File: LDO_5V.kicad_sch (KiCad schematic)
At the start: 36 parts, among them Q1601 NMOS, Q1602 NMOS, Q1603 NMOS, U1601 TPS62933, U1602 TPS62933, U1603 LM74700, U1604 LM74700

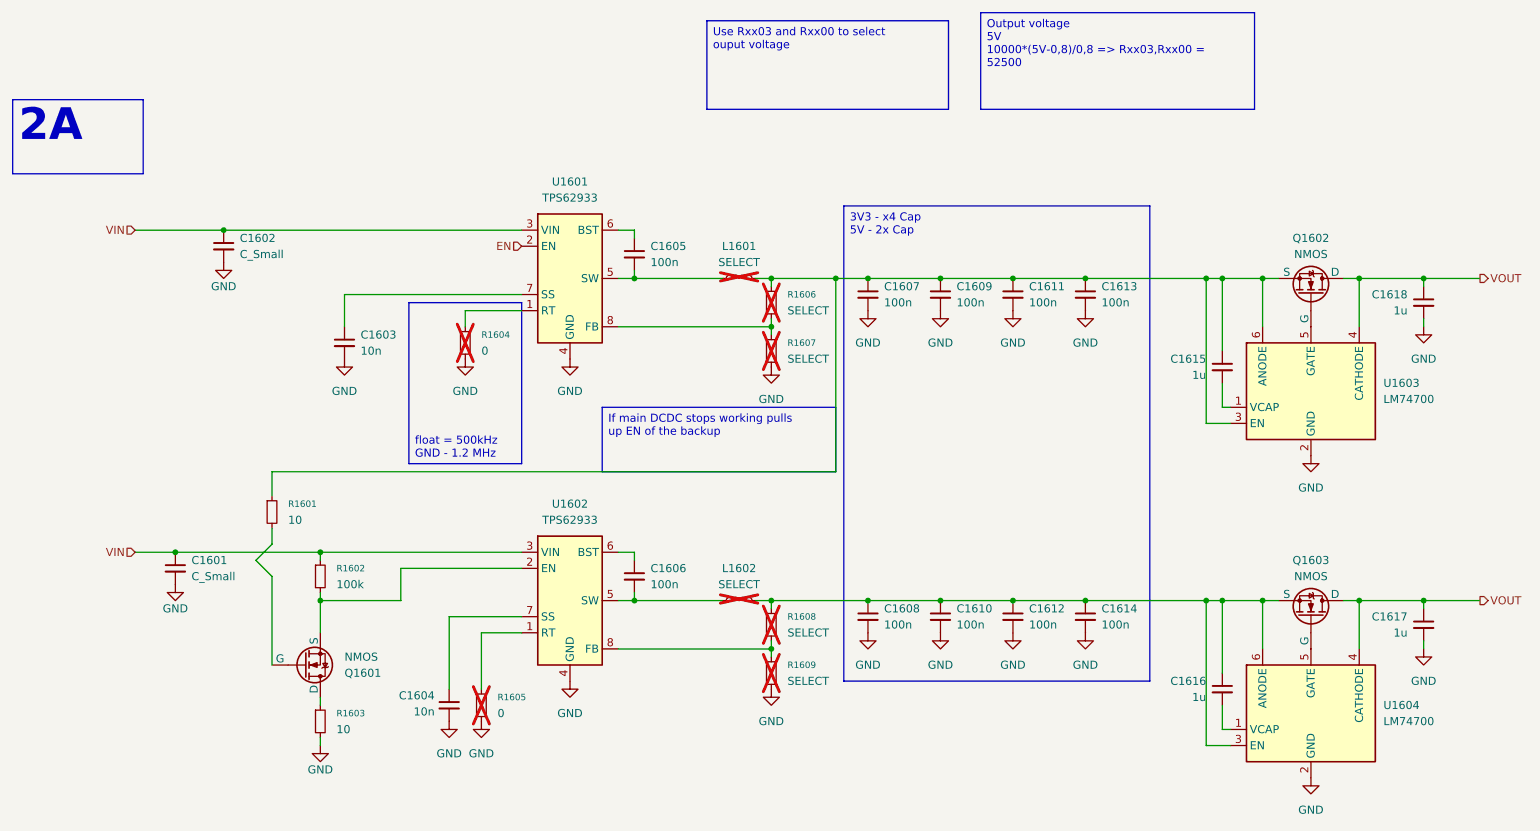
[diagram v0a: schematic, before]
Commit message: wired channel alerts; added schematic for test pbc
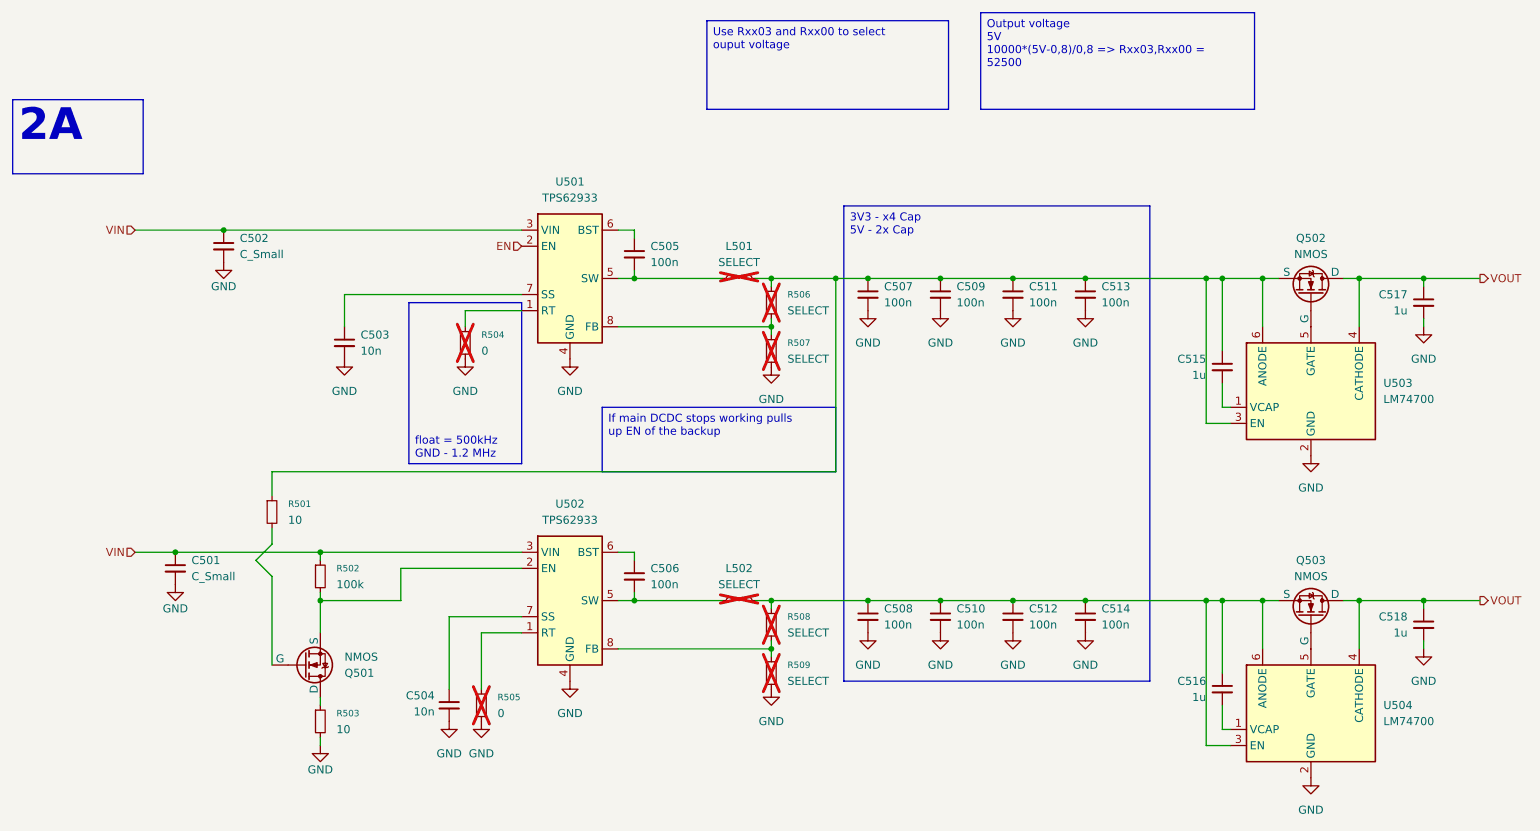
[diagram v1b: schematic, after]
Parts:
- removed C1601, C1602: C_Small, Capacitor_SMD:C_0603_1608Metric_Pad1.08x0.95mm_HandSolder, symbol Device:C_Small
- removed C1603, C1604: 10n, Capacitor_SMD:C_0603_1608Metric_Pad1.08x0.95mm_HandSolder, symbol Device:C_Small
- removed C1605, C1606, C1607, C1608, C1609, C1610, C1611, C1612, C1613, C1614: 100n, Capacitor_SMD:C_0603_1608Metric_Pad1.08x0.95mm_HandSolder, symbol Device:C_Small
- removed C1615, C1616, C1617, C1618: 1u, Capacitor_SMD:C_0603_1608Metric_Pad1.08x0.95mm_HandSolder, symbol Device:C_Small
- removed L1601, L1602: SELECT, Inductor_SMD:L_Taiyo-Yuden_NR-10050_9.8x10.0mm_HandSoldering, symbol Device:L_Small
- removed Q1601: NMOS, Package_TO_SOT_SMD:SOT-23, symbol Simulation_SPICE:NMOS
- removed Q1602, Q1603: NMOS, Package_TO_SOT_SMD:SOT-23-6, symbol Simulation_SPICE:NMOS
- removed R1601, R1603: 10, Resistor_SMD:R_0603_1608Metric_Pad0.98x0.95mm_HandSolder, symbol Device:R_Small
- removed R1602: 100k, Resistor_SMD:R_0603_1608Metric_Pad0.98x0.95mm_HandSolder, symbol Device:R_Small
- removed R1604, R1605: 0, Resistor_SMD:R_0603_1608Metric_Pad0.98x0.95mm_HandSolder, symbol Device:R_Small
- removed R1606, R1607, R1608, R1609: SELECT, Resistor_SMD:R_0603_1608Metric_Pad0.98x0.95mm_HandSolder, symbol Device:R_Small
- removed U1601, U1602: TPS62933, Package_TO_SOT_SMD:SOT-583-8, symbol Regulator_Switching:TPS62933
- removed U1603, U1604: LM74700, Package_TO_SOT_SMD:SOT-23-6, symbol Power_Management:LM74700
- added C501, C502: C_Small, Capacitor_SMD:C_0603_1608Metric_Pad1.08x0.95mm_HandSolder, symbol Device:C_Small
- added C503, C504: 10n, Capacitor_SMD:C_0603_1608Metric_Pad1.08x0.95mm_HandSolder, symbol Device:C_Small
- added C505, C506, C507, C508, C509, C510, C511, C512, C513, C514: 100n, Capacitor_SMD:C_0603_1608Metric_Pad1.08x0.95mm_HandSolder, symbol Device:C_Small
- added C515, C516, C517, C518: 1u, Capacitor_SMD:C_0603_1608Metric_Pad1.08x0.95mm_HandSolder, symbol Device:C_Small
- added L501, L502: SELECT, Inductor_SMD:L_Taiyo-Yuden_NR-10050_9.8x10.0mm_HandSoldering, symbol Device:L_Small
- added Q501: NMOS, Package_TO_SOT_SMD:SOT-23, symbol Simulation_SPICE:NMOS
- added Q502, Q503: NMOS, Package_TO_SOT_SMD:SOT-23-6, symbol Simulation_SPICE:NMOS
- added R501, R503: 10, Resistor_SMD:R_0603_1608Metric_Pad0.98x0.95mm_HandSolder, symbol Device:R_Small
- added R502: 100k, Resistor_SMD:R_0603_1608Metric_Pad0.98x0.95mm_HandSolder, symbol Device:R_Small
- added R504, R505: 0, Resistor_SMD:R_0603_1608Metric_Pad0.98x0.95mm_HandSolder, symbol Device:R_Small
- added R506, R507, R508, R509: SELECT, Resistor_SMD:R_0603_1608Metric_Pad0.98x0.95mm_HandSolder, symbol Device:R_Small
- added U501, U502: TPS62933, Package_TO_SOT_SMD:SOT-583-8, symbol Regulator_Switching:TPS62933
- added U503, U504: LM74700, Package_TO_SOT_SMD:SOT-23-6, symbol Power_Management:LM74700
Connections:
- net EN: now also U501.2 (EN)
- net GND: now also C501.2, C502.2, C503.2, C504.2, C507.2, C508.2, C509.2, C510.2, C511.2, C512.2, C513.2, C514.2, C517.2, C518.2, R503.2, R504.1, R505.1, R507.1, R509.1, U501.4 (GND), U502.4 (GND), U503.2 (GND), U504.2 (GND)
- net VIN: now also C501.1, C502.1, R502.1, U501.3 (VIN), U502.3 (VIN)
- net VOUT: now also C517.1, C518.1, Q502.1 (D), Q503.1 (D), U503.4 (CATHODE), U504.4 (CATHODE)
- new net: C508.1, C510.1, C512.1, C514.1, C516.1, L502.2, Q503.3 (S), R508.2, U504.3 (EN), U504.6 (ANODE)
- new net: C504.1, U502.7 (SS)
- new net: C503.1, U501.7 (SS)
- new net: R506.1, R507.2, U501.8 (FB)
- new net: Q501.3 (S), R502.2, U502.2 (EN)
- new net: Q503.2 (G), U504.5 (GATE)
- new net: C507.1, C509.1, C511.1, C513.1, C515.1, L501.2, Q502.3 (S), R501.1, R506.2, U503.3 (EN), U503.6 (ANODE)
- new net: C516.2, U504.1 (VCAP)
- new net: Q502.2 (G), U503.5 (GATE)
- new net: R504.2, U501.1 (RT)
- new net: R505.2, U502.1 (RT)
- new net: C506.2, L502.1, U502.5 (SW)
- new net: C506.1, U502.6 (BST)
- new net: R508.1, R509.2, U502.8 (FB)
- new net: Q501.1 (D), R503.1
- new net: Q501.2 (G), R501.2
- new net: C505.2, L501.1, U501.5 (SW)
- new net: C515.2, U503.1 (VCAP)
- new net: C505.1, U501.6 (BST)

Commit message: reduced number of DCDC converter for PV panels; updated test pcb
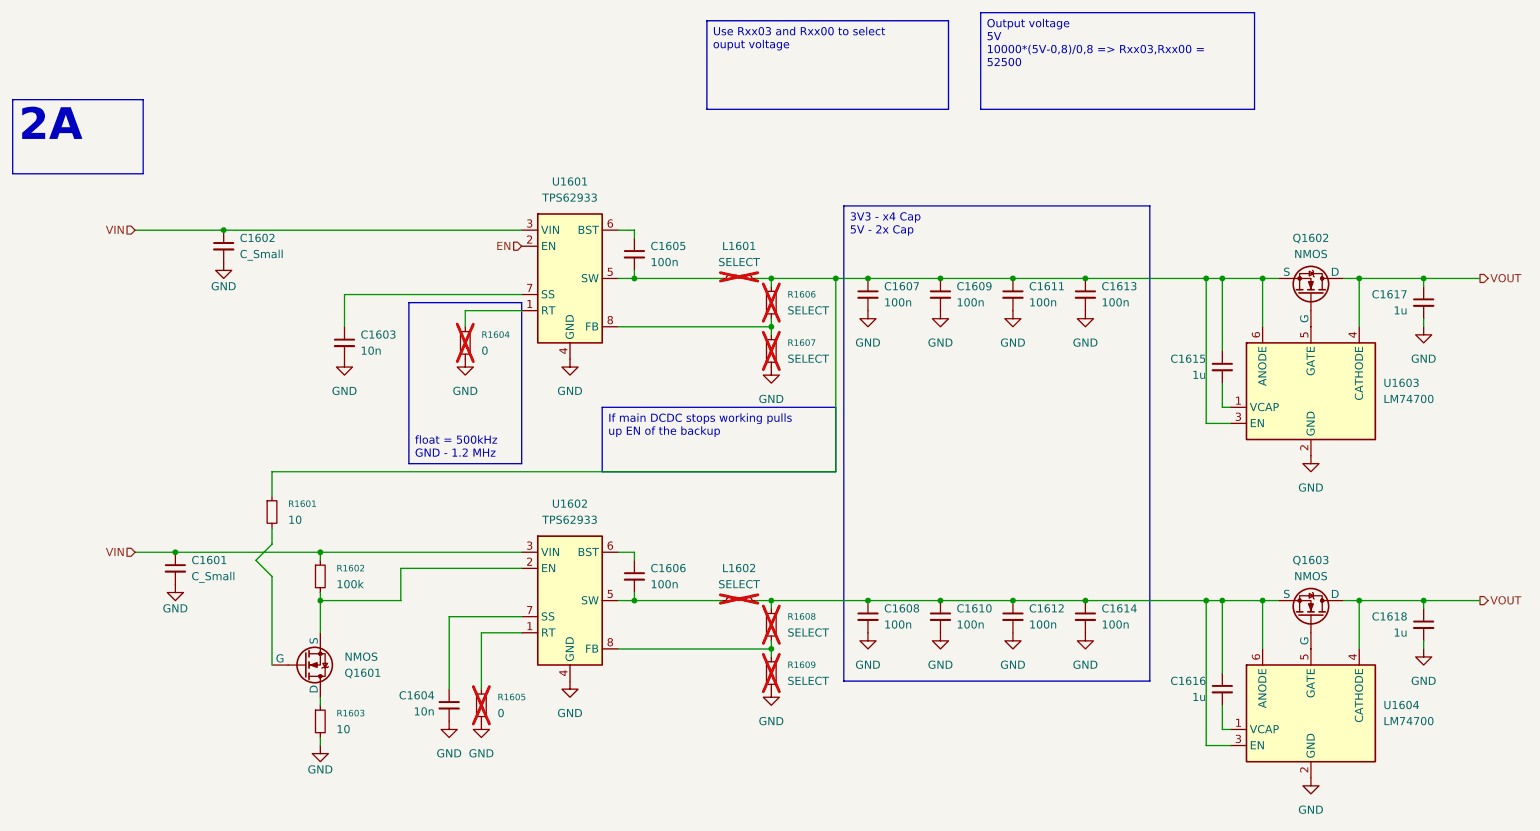
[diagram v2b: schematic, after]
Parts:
- L1601: renamed from L501; footprint Inductor_SMD:L_Taiyo-Yuden_NR-10050_9.8x10.0mm_HandSoldering -> Inductor_SMD:L_6.3x6.3_H3
- L1602: renamed from L502; footprint Inductor_SMD:L_Taiyo-Yuden_NR-10050_9.8x10.0mm_HandSoldering -> Inductor_SMD:L_6.3x6.3_H3
- Q1602: renamed from Q502; footprint Package_TO_SOT_SMD:SOT-23-6 -> Outlines:NVTFS5116PLTWG
- Q1603: renamed from Q503; footprint Package_TO_SOT_SMD:SOT-23-6 -> Outlines:NVTFS5116PLTWG
- renumbered C501 to C1601, C502 to C1602, C503 to C1603, C504 to C1604, C505 to C1605, C506 to C1606, C507 to C1607, C508 to C1608, C509 to C1609, C510 to C1610, C511 to C1611, C512 to C1612, C513 to C1613, C514 to C1614, C515 to C1615, C516 to C1616, C517 to C1617, C518 to C1618, Q501 to Q1601, R501 to R1601, R502 to R1602, R503 to R1603, R504 to R1604, R505 to R1605, R506 to R1606, R507 to R1607, R508 to R1608, R509 to R1609, U501 to U1601, U502 to U1602, U503 to U1603, U504 to U1604
